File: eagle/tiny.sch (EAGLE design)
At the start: 29 parts, among them Q3 16MHz, T1 2N3565, T2 2N3565, U1 ATTINY48-MU

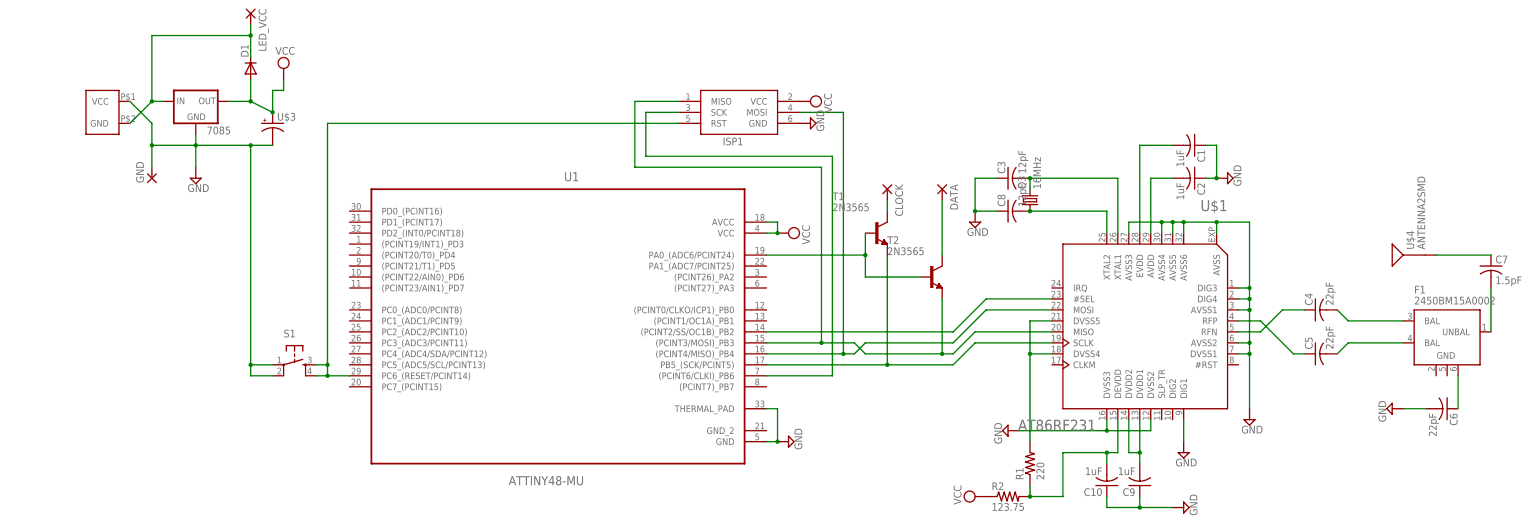
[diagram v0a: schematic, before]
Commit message: Make a tiny prototype of skylighting
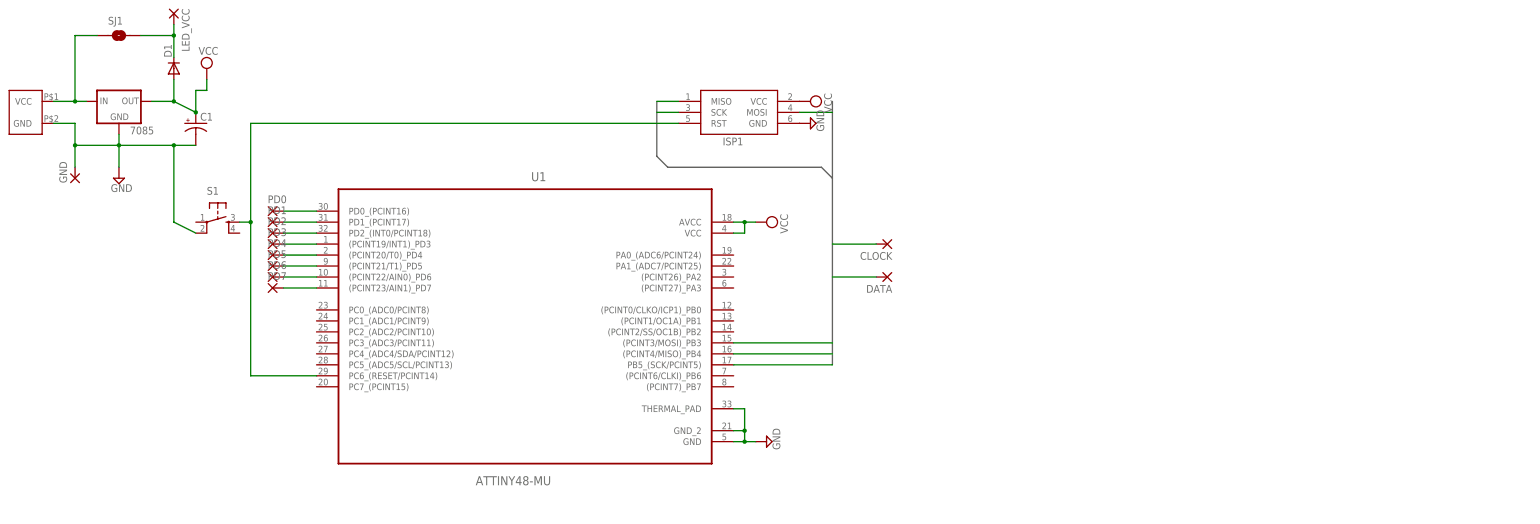
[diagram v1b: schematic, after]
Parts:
- removed C10, C2, C9: 1uF, adafruit:C-US025-030X050
- removed C3, C8: 12pF, adafruit:C-US025-030X050
- removed C4, C5, C6: 22pF, adafruit:C-US025-030X050
- removed C7: 1.5pF, adafruit:C-US025-030X050
- removed F1: 2450BM15A0002, johanson-technology:2450BM15A0002
- removed Q3: 16MHz, adafruit:CRYSTALCTS406
- removed R1: 220, adafruit:R-US_0204/7
- removed R2: 123.75, adafruit:R-US_0204/7
- removed T1, T2: 2N3565, transistor:2N3565
- removed U$1: AT86RF231, at86rf231:AT86RF231
- removed U$3: (no value), adafruit:CPOL-USE2.5-6
- removed U$4: ANTENNA2SMD, SparkFun:ANTENNA2SMD
- added PD0, PD1, PD2, PD3, PD4, PD5, PD6, PD7: (no value), wirepad:1,6/0,9
- added SJ1: LED_VCC = VCC, SparkFun:SOLDERJUMPERNO
- C1: value 1uF -> (none); device adafruit:C-US025-030X050 -> adafruit:CPOL-USE2.5-6
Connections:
- removed net AVDD: C2.2, U$1.AVDD
- removed net DEVDD: C10.2, R1.1, R2.2, U$1.DEVDD
- removed net DVDD2: C9.2, U$1.DVDD1, U$1.DVDD2
- removed net EVDD: C1.2, U$1.EVDD
- removed net N$1: T1.B, T2.B, U1.PA0_(ADC6/PCINT24)
- removed net N$10: C5.2, F1.BAL@2
- removed net N$11: T1.E, U$1.SCLK, U1.PB5_(SCK/PCINT5)
- removed net N$12: DATA.P, T2.C
- removed net N$13: ISP1.SCK, U1.(PCINT6/CLKI)_PB6
- removed net N$14: C4.1, U$1.RFN
- removed net N$15: C8.2, Q3.1, U$1.XTAL2
- removed net N$16: C3.2, Q3.2, U$1.XTAL1
- removed net N$17: R1.2, U$1.DVSS4, U$1.DVSS5
- removed net N$18: C7.2, F1.UNBAL
- removed net N$2: C5.1, U$1.RFP
- removed net N$23: C6.1, F1.GND@3
- removed net N$24: C7.1, U$4.SIGNAL
- removed net N$3: ISP1.MOSI, U$1.MOSI, U1.(PCINT4/MISO)_PB4
- removed net N$5: CLOCK.P, T1.C
- removed net N$8: C4.2, F1.BAL@1
- removed net N$9: U$1.#SEL, U1.(PCINT2/SS/OC1B)_PB2
- new net MISO: ISP1.MISO, U1.(PCINT4/MISO)_PB4
- new net N$32: PD0.P, U1.PD0_(PCINT16)
- new net N$33: PD1.P, U1.PD1_(PCINT17)
- new net N$34: PD2.P, U1.PD2_(INT0/PCINT18)
- new net N$35: PD3.P, U1.(PCINT19/INT1)_PD3
- new net N$36: PD4.P, U1.(PCINT20/T0)_PD4
- new net N$37: PD5.P, U1.(PCINT21/T1)_PD5
- new net N$38: PD6.P, U1.(PCINT22/AIN0)_PD6
- new net N$39: PD7.P, U1.(PCINT23/AIN1)_PD7
- new net N$40: D1.C, LED_VCC.P, SJ1.2
- new net SCK: CLOCK.P, ISP1.SCK, U1.PB5_(SCK/PCINT5)
- net GND: now also C1.-, U1.GND_2, VCC.GND; no longer C1.1, C10.1, C2.1, C3.1, C6.2, C8.1, C9.1, S1.1, U$1.AVSS, U$1.AVSS1, U$1.AVSS2, U$1.AVSS3, U$1.AVSS4, U$1.AVSS5, U$1.AVSS6, U$1.DIG1, U$1.DIG3, U$1.DIG4, U$1.DVSS1, U$1.DVSS2, U$1.DVSS3, U$3.-, VCC.VCC
- net MOSI: now also DATA.P, ISP1.MOSI; no longer ISP1.MISO, T2.E, U$1.MISO
- net N$4: no longer S1.4
- net N$6: now also SJ1.1, VCC.VCC; no longer D1.C, LED_VCC.P, VCC.GND
- net VCC: now also C1.+; no longer R2.1, U$3.+
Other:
- moved on the sheet: 7085, CLOCK, D1, DATA, GND, LED_VCC, S1, U1
